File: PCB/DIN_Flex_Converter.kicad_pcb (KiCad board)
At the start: 2 copper layers, 14 parts

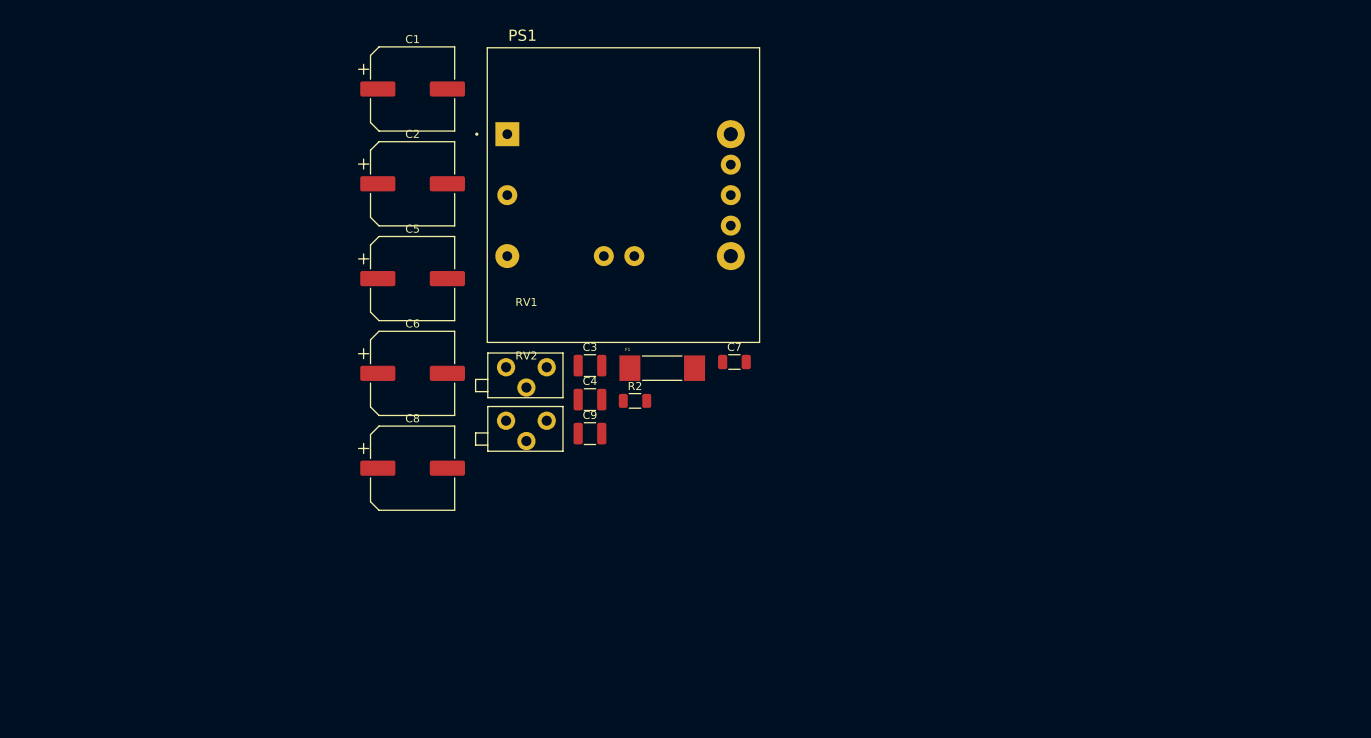
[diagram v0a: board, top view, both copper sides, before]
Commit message: Added Indication Ckt to Schematic
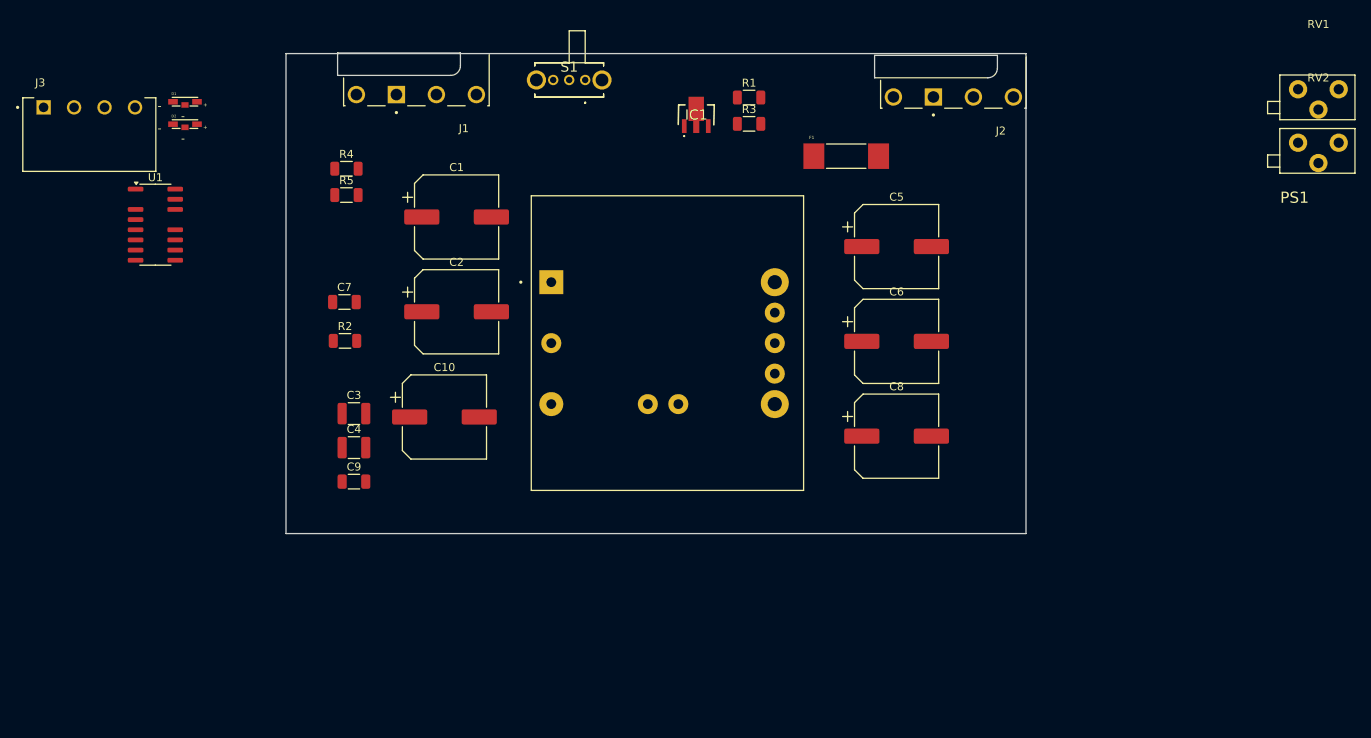
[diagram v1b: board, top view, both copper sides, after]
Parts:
- added C10: 180uF, Capacitor_SMD:CP_Elec_10x12.6, F.Cu at (132.3, 97.9)
- added D1: LED GRN, PSA:LED_155124RV73200, F.Cu at (99.9, 58.5)
- added D2: LED RED, PSA:LED_155124RV73200, F.Cu at (99.9, 61.3)
- added IC1: ZXTR2005Z-13, PSA:AZ7042RTRG1, F.Cu at (163.8, 60.2)
- added J1: Screw_Terminal_01x04, PSA:PHOENIX_2200320, F.Cu at (137.9, 40.2)
- added J2: Screw_Terminal_01x04, PSA:PHOENIX_2200320, F.Cu at (205.0, 40.5)
- added J3: Conn_01x04_Socket, PSA:PHOENIX_1803293, F.Cu at (79.6, 67.2)
- added R1: 1k, Resistor_SMD:R_1206_3216Metric, F.Cu at (170.4, 58.0)
- added R3: 1k, Resistor_SMD:R_1206_3216Metric, F.Cu at (170.4, 61.3)
- added R4: 10k, Resistor_SMD:R_1206_3216Metric, F.Cu at (120.1, 66.9)
- added R5: 10k, Resistor_SMD:R_1206_3216Metric, F.Cu at (120.1, 70.2)
- added S1: EG1247, PSA:EG1247, F.Cu at (149.9, 55.8)
- added U1: 74HC04, Package_SO:SOIC-14-16_3.9x9.9mm_P1.27mm, F.Cu at (96.2, 73.9)
- C1, C2: value 270uF -> 180uF
- C9: footprint Capacitor_SMD:C_1210_3225Metric -> Capacitor_SMD:C_1206_3216Metric
- moved RV1 104.9 mm to (241.6, 59.5)
- moved RV2 104.9 mm to (241.6, 66.2)
- moved C5 60.6 mm to (188.8, 76.6)
- moved C6 60.6 mm to (188.8, 88.5)
- moved C8 60.6 mm to (188.8, 100.3)
- moved C7 49.3 mm to (119.8, 83.6)
- moved R2 37.0 mm to (119.9, 88.4)
- moved F1 35.1 mm to (182.5, 65.3)
- moved C3 30.1 mm to (121.0, 97.5)
- moved C4 30.1 mm to (121.0, 101.8)
- moved C9 30.1 mm to (121.0, 106.0)
- moved PS1 19.3 mm to (145.7, 81.1)
- moved C1 16.9 mm to (133.8, 72.9)
- moved C2 16.9 mm to (133.8, 84.8)
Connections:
- net Net-(PS1-VIN(+)) renamed /PWR_IN_PROT
- C7 pad 1: /COMP PWR CM -> /I_MON
- PS1 pad 34: /COMP PWR CM -> Net-(PS1-CURRENT_MONITOR)
- PS1 pad 5: unconnected-(PS1-PWR_GOOD-Pad5) -> /~{PWR_GOOD}
- PS1 pad 6: Net-(PS1-TRIM) -> /Trim
- R2 pad 1: GND -> /I_MON
- R2 pad 2: /COMP PWR CM -> Net-(PS1-CURRENT_MONITOR)
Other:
- board outline added: 92.5 x 60 mm

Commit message: Draft Schematic & Layout
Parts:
- added H1: MountingHole, MountingHole:MountingHole_3.2mm_M3_DIN965, F.Cu at (119.0, 71.6)
- added H2: MountingHole, MountingHole:MountingHole_3.2mm_M3_DIN965, F.Cu at (108.0, 130.6)
- added H3: MountingHole, MountingHole:MountingHole_3.2mm_M3_DIN965, F.Cu at (173.0, 71.6)
- added H4: MountingHole, MountingHole:MountingHole_3.2mm_M3_DIN965, F.Cu at (184.0, 130.6)
- added J4: Conn_02x06_Top_Bottom, Connector_PinSocket_2.54mm:PinSocket_2x06_P2.54mm_Vertical_SMD, F.Cu at (111.8, 101.5)
- added J5: Conn_02x06_Top_Bottom, Connector_PinSocket_2.54mm:PinSocket_2x06_P2.54mm_Vertical_SMD, B.Cu at (111.8, 101.5)
- J1: footprint PSA:PHOENIX_2200320 -> PSA:PHOENIX_2907774
- J2: footprint PSA:PHOENIX_2200320 -> PSA:PHOENIX_2907787
- RV1, RV2: footprint PSA:Bourns PV37X -> PSA:3009P1154LF
- moved RV2 116.0 mm to (126.6, 81.7), turned to 90 degrees
- moved RV1 98.6 mm to (145.4, 81.7), turned to 90 degrees
- moved J3 89.5 mm to (169.0, 63.5), turned to 180 degrees
- moved U1 68.0 mm to (163.9, 79.5)
- moved F1 59.9 mm to (127.8, 89.7)
- moved C9 54.5 mm to (172.3, 87.4), turned to 90 degrees
- moved J2 52.0 mm to (186.6, 89.2), turned to 65 degrees
- moved J1 51.8 mm to (97.6, 72.8), turned to -65 degrees
- moved C1 50.3 mm to (128.2, 122.9), turned to 180 degrees
- moved R3 40.6 mm to (132.9, 77.0), turned to -90 degrees
- moved R1 39.7 mm to (135.5, 77.0), turned to -90 degrees
- moved R2 37.0 mm to (156.1, 80.7), turned to 180 degrees
- moved R4 37.0 mm to (156.1, 75.2)
- moved R5 36.8 mm to (156.1, 78.0)
- moved C7 36.4 mm to (156.2, 83.4), turned to 180 degrees
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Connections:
- net Net-(J1-Pin_3) renamed /PWR_IN
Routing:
- added copper zone on F.Cu, net /PWR OUT
- added copper zone on F.Cu, net /PWR_IN
- added copper zone on F.Cu, net /PWR_IN_PROT
- added copper zone on B.Cu, net GND
- added copper zone on F.Cu, net GND
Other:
- board size 92.5 x 60 mm -> 88.5 x 70 mm
